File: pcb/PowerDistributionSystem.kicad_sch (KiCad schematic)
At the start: 0 parts

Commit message: Schematic'ing out the TMC2209.
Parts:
- added C1, C2, C4, C8: 100n, symbol Device:C_Small
- added C3: 100u, symbol Device:C_Polarized
- added C5: 2u2, symbol Device:C_Small
- added C6: 22n, symbol Device:C_Small
- added D1: YELLOW, symbol Device:LED
- added R1, R2: 50m, symbol Device:R
- added R3: 2k, symbol Device:R
- added R4: 1k, symbol Device:R
- added R5: 20k, symbol Device:R
- added R6: 33k, symbol Device:R
- added R7: 10k, symbol Device:R_Variable
- added TP1, TP2, TP3: TestPoint, symbol Connector:TestPoint
- added U1: TMC2209-LA-T, Package_DFN_QFN:VQFN-28-1EP_5x5mm_P0.5mm_EP3.7x3.7mm_ThermalVias, symbol Driver_Motor:TMC2209-LA
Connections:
- new net: R4.1, TP1.1, U1.14 (~{PD}/UART)
- new net: C6.1, U1.4 (CPO)
- new net: C6.2, U1.5 (CPI)
- new net: R2.2, U1.27 (BRB)
- new net: C5.1, R6.2, U1.8 (5VOUT)
- new net: R1.2, U1.23 (BRA)
- new net: C4.2, U1.6 (VCP)
- new net +3.3V: C8.1, R5.2, U1.15 (VCC_IO)
- new net +BATT: C1.1, C2.1, C3.1, C4.1, U1.22 (VS), U1.28 (VS)
- new net GND: C1.2, C2.2, C3.2, C5.2, C8.2, D1.1 (K), R1.1, R2.1, R7.2, U1.13 (CLK), U1.18 (GND), U1.25 (NC), U1.29 (GND), U1.3 (GND)
- new net MOTOR_DRIVER_A1: U1.24 (OA1)
- new net MOTOR_DRIVER_A2: U1.21 (OA2)
- new net MOTOR_DRIVER_B1: U1.26 (OB1)
- new net MOTOR_DRIVER_B2: U1.1 (OB2)
- new net MOTOR_DRIVER_DIAGNOSTIC: TP2.1, U1.11 (DIAG)
- new net MOTOR_DRIVER_DIR: U1.19 (DIR)
- new net MOTOR_DRIVER_ENABLE: R5.1, U1.2 (~{EN})
- new net MOTOR_DRIVER_INDEX: TP3.1, U1.12 (INDEX)
- new net MOTOR_DRIVER_MICROSTEP_1: U1.9 (MS1/AD0)
- new net MOTOR_DRIVER_MICROSTEP_2: U1.10 (MS2/AD1)
- new net MOTOR_DRIVER_SPREAD: U1.7 (SPREAD)
- new net MOTOR_DRIVER_STEP: R3.2, U1.16 (STEP)
- new net MOTOR_DRIVER_STEP_LED_ANODE: D1.2 (A), R3.1
- new net MOTOR_DRIVER_UART: R4.2
- new net MOTOR_DRIVER_VREF: R6.1, R7.1, U1.17 (VREF)
- no-connect marks 0 -> 1
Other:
- note added: ""Attach 2.2μF to 4.7μF ceramic capacitor to GND near to pin for best performance." Note that Adafruit deviates and uses 10uF. @/pg 4/fig 1.1/`TMC2209`. @/pg 9/tbl 2.2/`TMC2209`."
- note added: ""Tie to CPO using 22nF 50V capacitor." @/pg 4/fig 1.1/`TMC2209`. @/pg 9/tbl 2.2/`TMC2209`."
- note added: ""Tie to GND using short wire for internal clock..." This is what the Adafruit breakout board also does. @/pg 8/sec 1.9/`TMC2209`. @/pg 9/tbl 2.2/`TMC2209`."
- note added: ""Tie to VS using 100nF capacitor." Note that Adafruit deviates from this by using 220nF for their breakout board instead. Not sure why. @/pg 4/fig 1.1/`TMC2209`. @/pg 9/tbl 2.2/`TMC2209`."
- note added: "@/pg 4/fig 1.1/`TMC2209`."
- note added: "Can be left unused according to Adafruit's design."
- note added: "Reference design: @/url:`github.com/adafruit/Adafruit-TMC2209-Breakout-PCB`."
- note added: "TODO: Low ESR."
- note added: "TODO: No 22nF in book."
- note added: "TODO: Not sure how important VREF is."
- note added: "TODO: Sense resistor? @/url:`digikey.com/en/products/detail/yageo/RL1206FR-070R05L/3885413`."
- note added: "TODO: Simplex UART? @/pg 82/fig 21.4/`TMC2209`."
- note added: "TODO: Tests should be done on what happens if the stepper motors are turned."

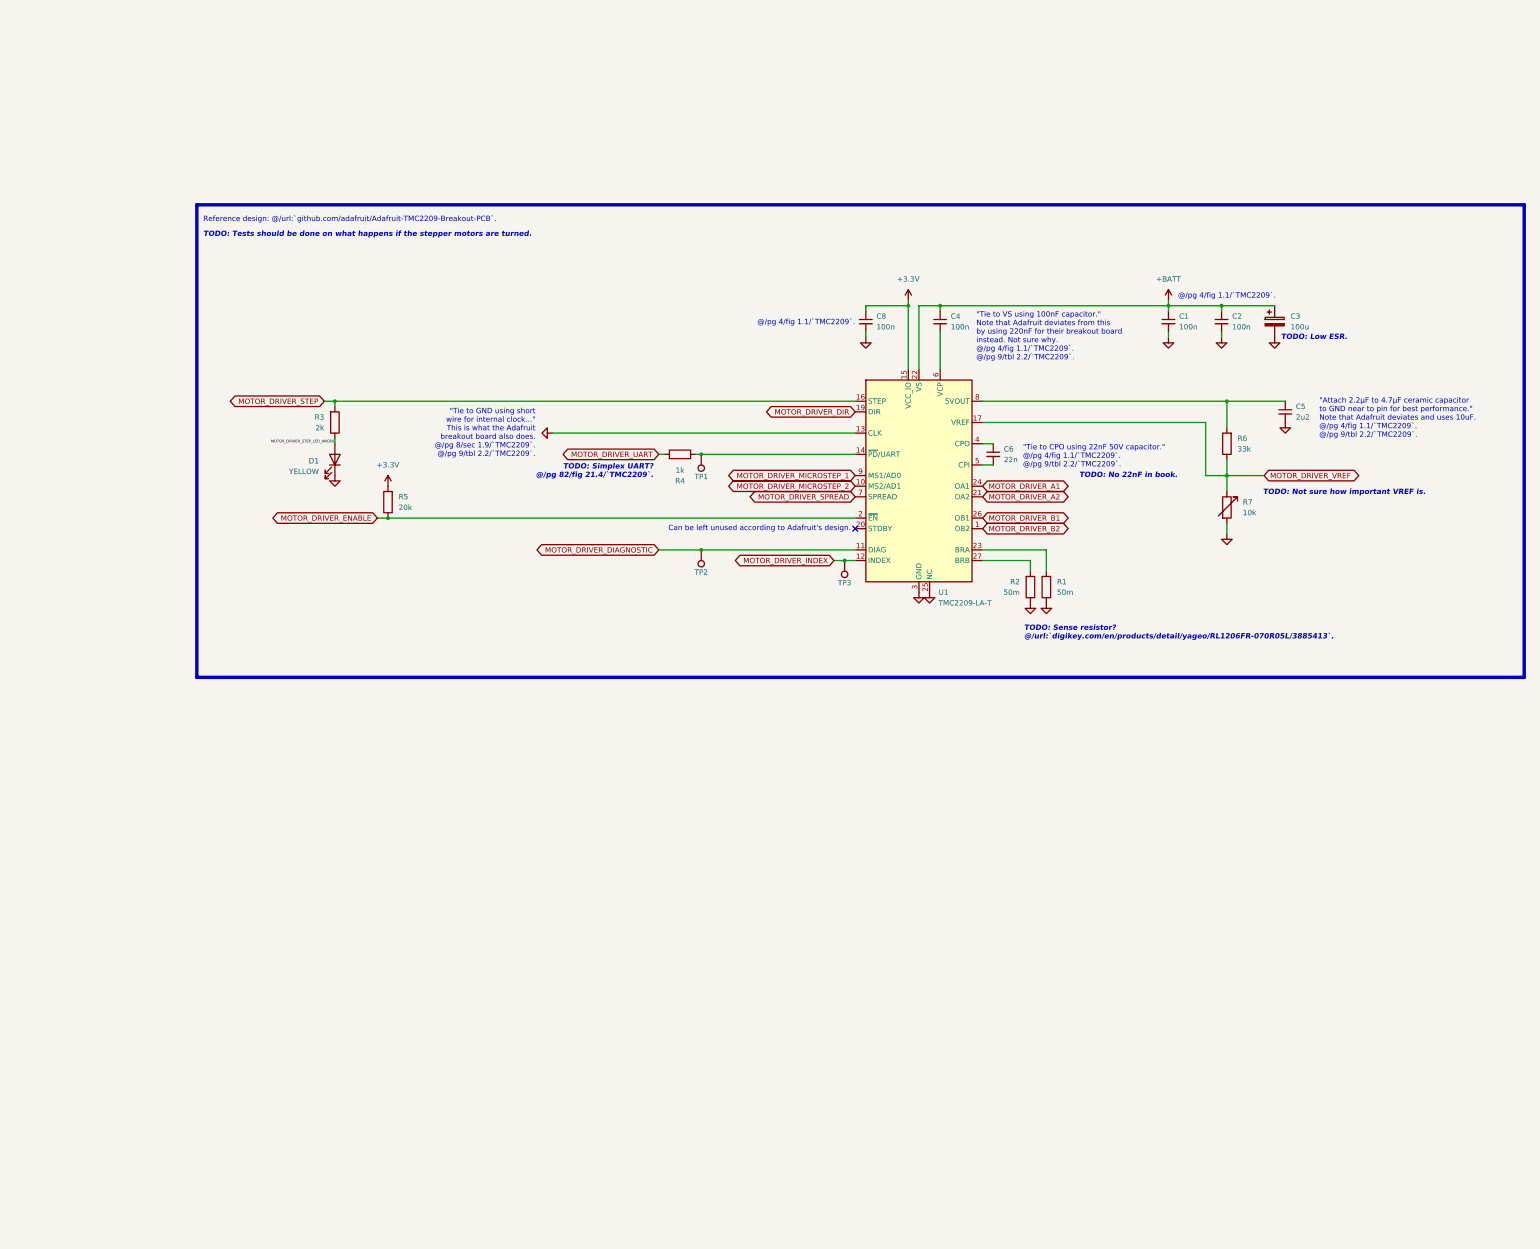
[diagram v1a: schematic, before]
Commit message: Added footprints for TMC2209, PDS housing, and edge-cuts.
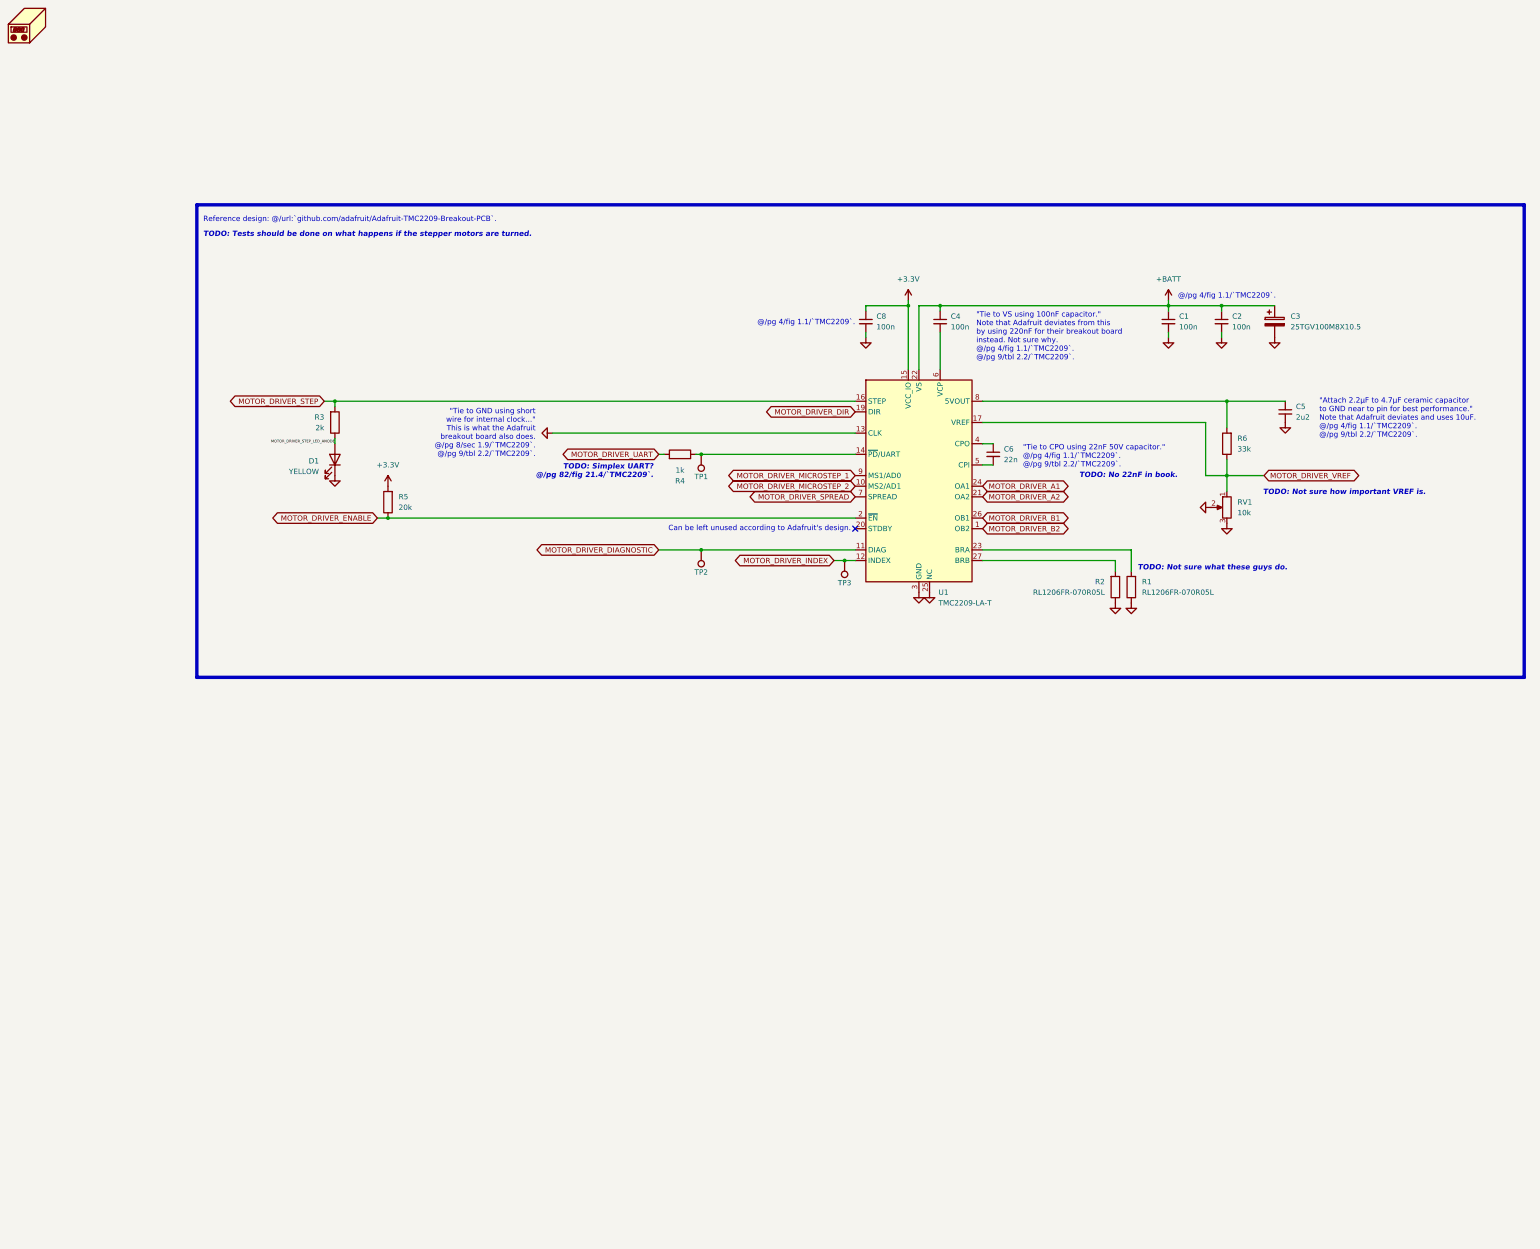
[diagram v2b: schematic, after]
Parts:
- removed R7: 10k, symbol Device:R_Variable
- added N1: Housing, pcb:PowerDistributionSystemHousing, symbol Mechanical:Housing
- added RV1: 10k, pcb:TRIM_35WR10KLFTR, symbol Device:R_Potentiometer
- C1, C2, C4, C5, C6, C8: footprint (none) -> Capacitor_SMD:C_1206_3216Metric_Pad1.33x1.80mm_HandSolder
- C3: value 100u -> 25TGV100M8X10.5; footprint (none) -> Capacitor_SMD:CP_Elec_8x10.5
- D1: footprint (none) -> LED_SMD:LED_1206_3216Metric_Pad1.42x1.75mm_HandSolder
- R1, R2: value 50m -> RL1206FR-070R05L; footprint (none) -> Resistor_SMD:R_1206_3216Metric_Pad1.30x1.75mm_HandSolder
- R3, R4, R5, R6: footprint (none) -> Resistor_SMD:R_1206_3216Metric_Pad1.30x1.75mm_HandSolder
- TP1, TP2, TP3: footprint (none) -> TestPoint:TestPoint_Pad_1.0x1.0mm
- U1: footprint Package_DFN_QFN:VQFN-28-1EP_5x5mm_P0.5mm_EP3.7x3.7mm_ThermalVias -> pcb:VQFN-28-1EP_5x5mm_P0.5mm_EP3.7x3.7mm_ThermalVias
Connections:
- net GND: now also RV1.2, RV1.3
- net MOTOR_DRIVER_VREF: now also RV1.1
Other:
- note added: "TODO: Not sure what these guys do."
- note removed: "TODO: Low ESR."
- note removed: "TODO: Sense resistor? @/url:`digikey.com/en/products/detail/yageo/RL1206FR-070R05L/3885413`."
- moved on the sheet: R1, R2

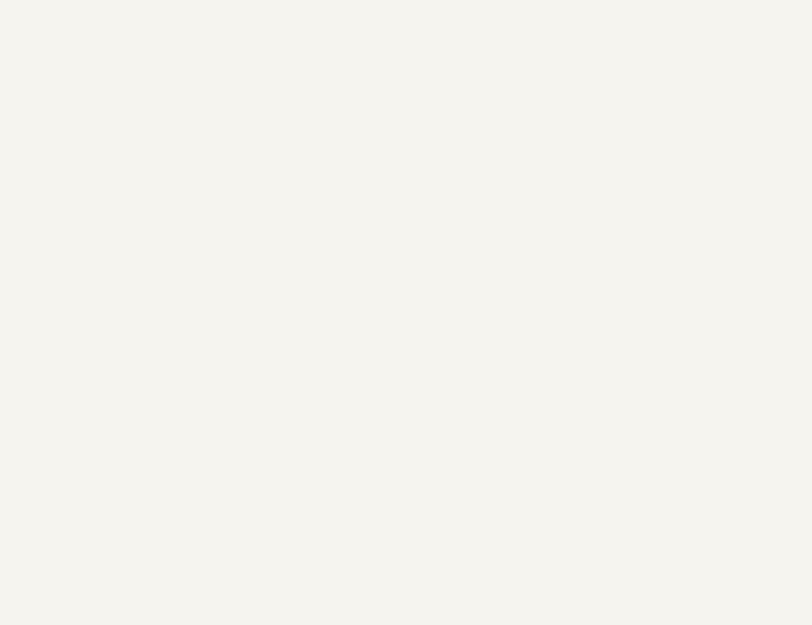
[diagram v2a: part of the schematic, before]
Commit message: Added placeholder connectors.
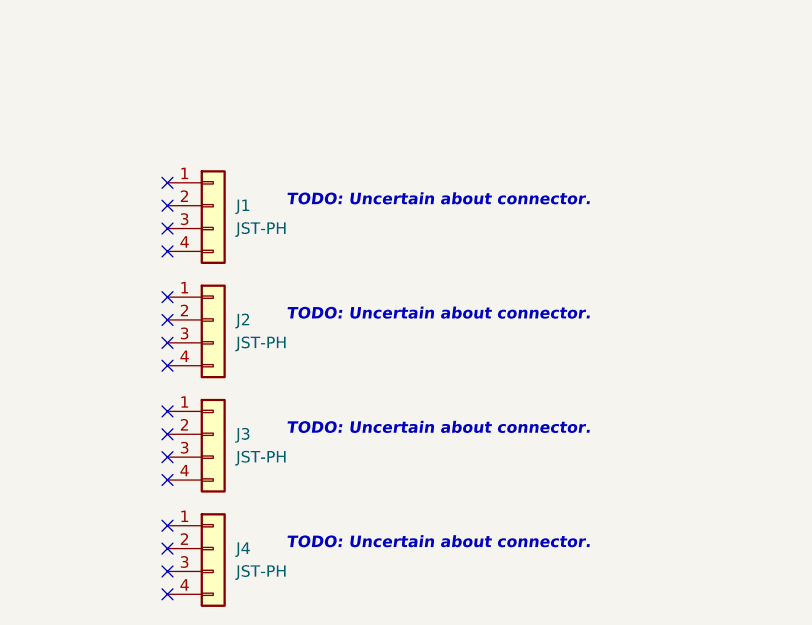
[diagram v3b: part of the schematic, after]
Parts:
- added J1, J2, J3, J4: JST-PH, Connector_JST:JST_PH_B4B-PH-K_1x04_P2.00mm_Vertical, symbol Connector_Generic:Conn_01x04
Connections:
- no-connect marks 1 -> 17
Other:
- note added: "TODO: Uncertain about connector."

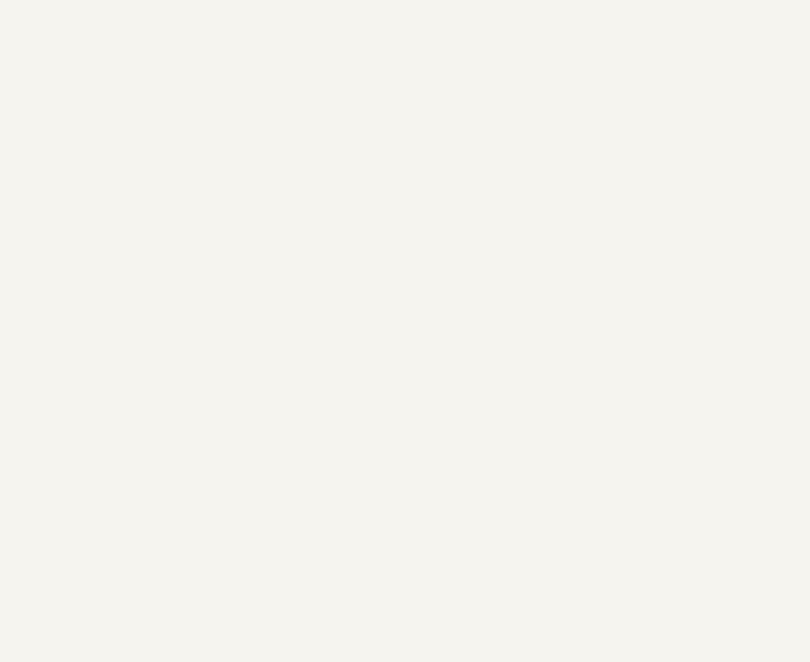
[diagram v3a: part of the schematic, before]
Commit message: Added symbols and footprints for D24V7Fx regulators.
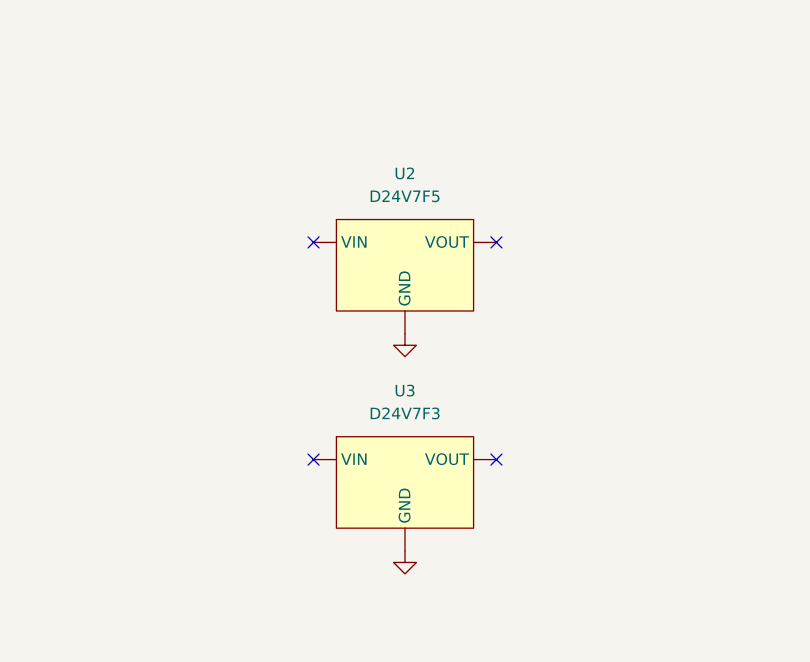
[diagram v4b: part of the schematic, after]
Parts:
- added U2: D24V7F5, pcb:D24V7Fx, symbol D24V7Fx:D24V7Fx
- added U3: D24V7F3, pcb:D24V7Fx, symbol D24V7Fx:D24V7Fx
- U1: footprint pcb:VQFN-28-1EP_5x5mm_P0.5mm_EP3.7x3.7mm_ThermalVias -> Package_DFN_QFN:VQFN-28-1EP_5x5mm_P0.5mm_EP3.7x3.7mm_ThermalVias
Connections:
- net GND: now also U2.GND, U3.GND
- no-connect marks 17 -> 21

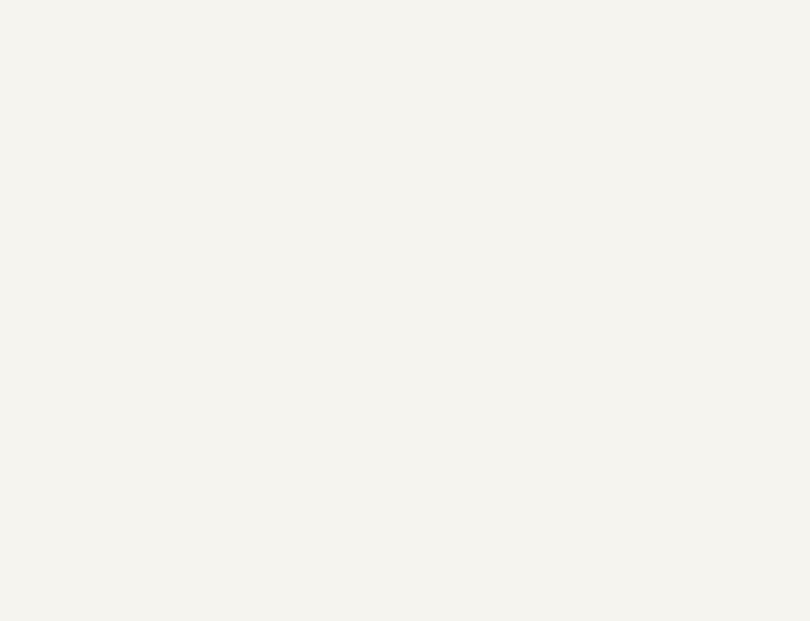
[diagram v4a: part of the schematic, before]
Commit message: Setting up a connection matrix.
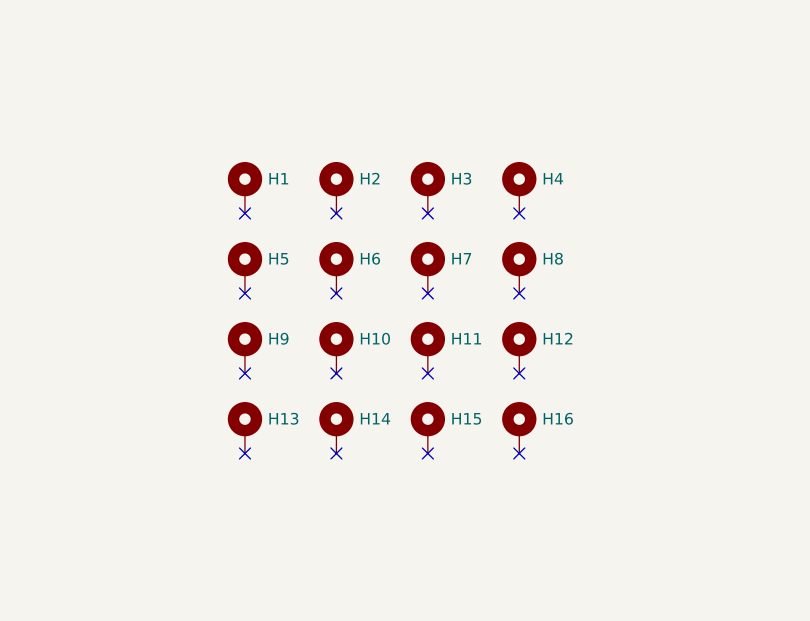
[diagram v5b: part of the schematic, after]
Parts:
- added H1, H10, H11, H12, H13, H14, H15, H16, H2, H3, H4, H5, H6, H7, H8, H9: MountingHole_Pad_MP, pcb:Matrix_Hole, symbol Mechanical:MountingHole_Pad_MP
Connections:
- no-connect marks 21 -> 37
